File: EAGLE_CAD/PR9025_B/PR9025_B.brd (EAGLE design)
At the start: 70 x 70 mm, 75 parts, among them SW1 C&K_PTS645

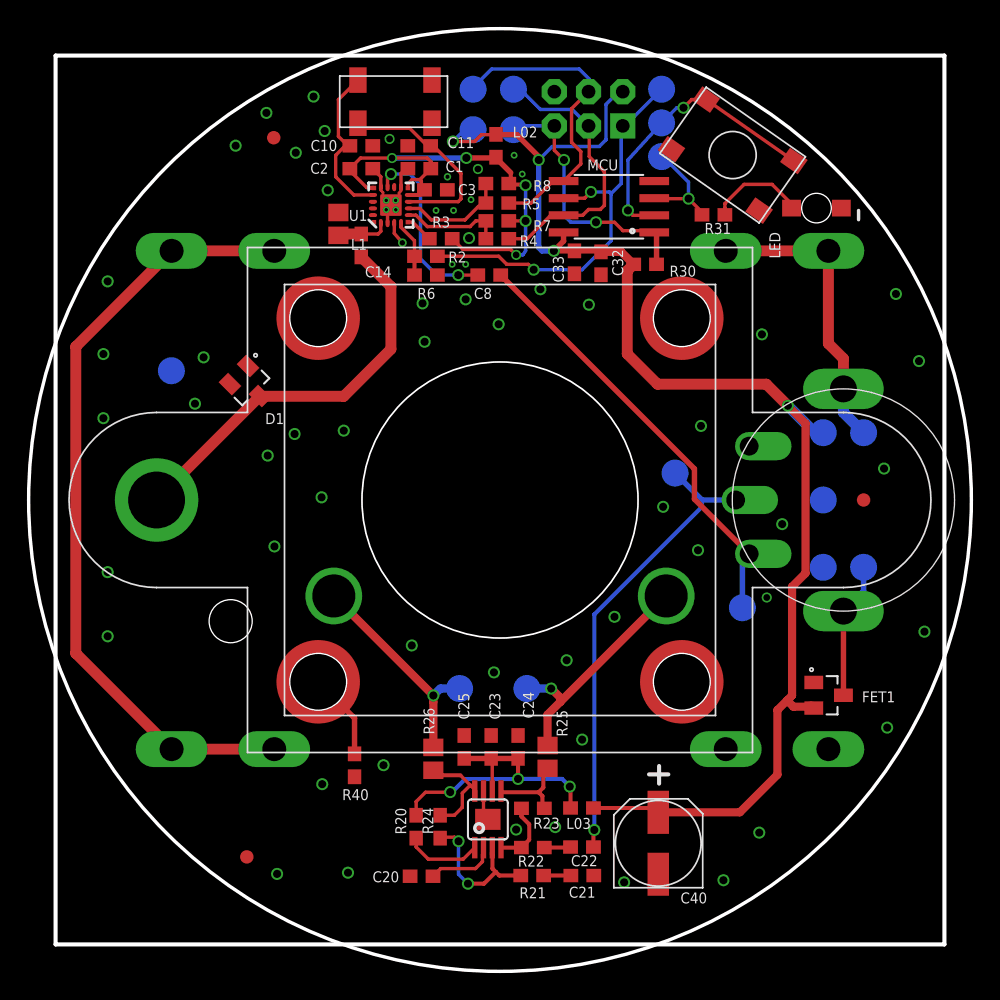
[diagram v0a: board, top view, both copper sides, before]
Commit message: PR9025_B
This is a WIP. 9025B will incorporate learnings from Josh’s 9025A
build, and most significantly update the ISP header to be centered on
the PCB at 35mm. There’s still routing and error checking to be done.
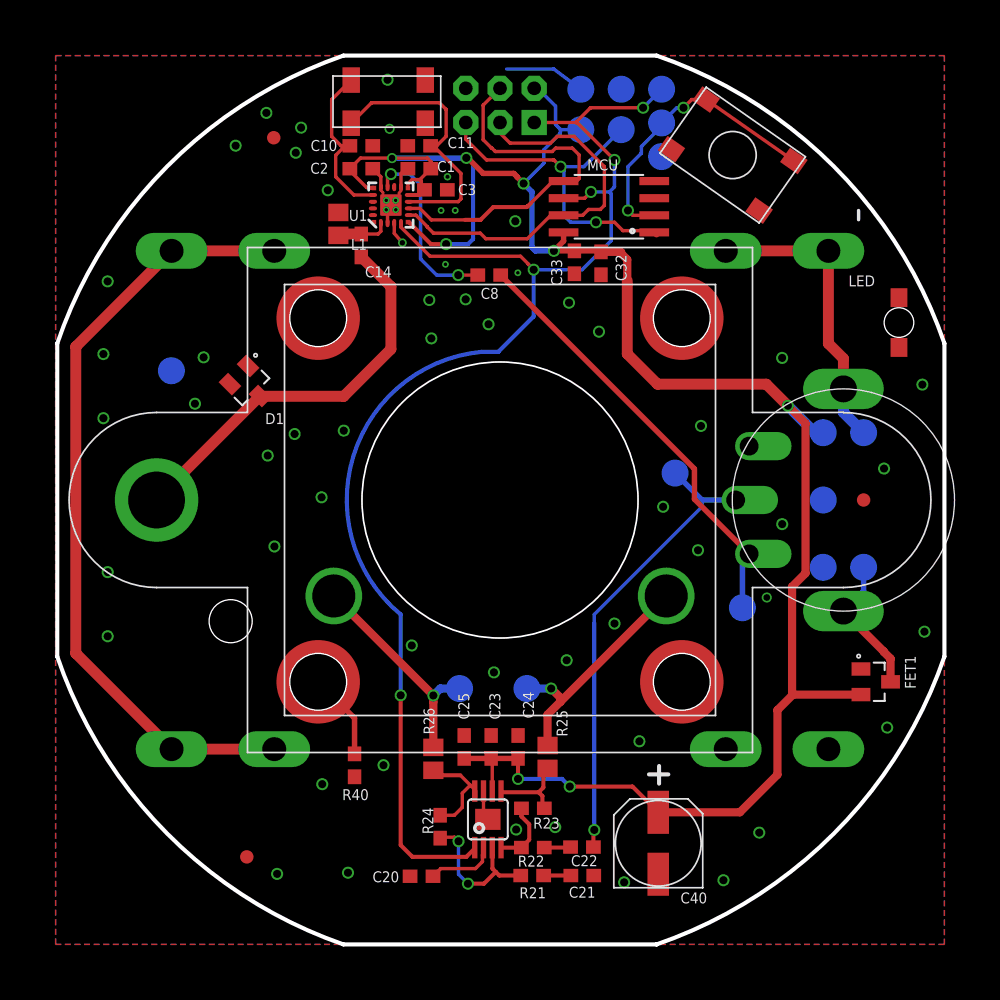
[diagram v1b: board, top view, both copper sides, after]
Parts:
- removed L02, L03: 2.2k@100MHz, PR_Parts_Library:0603_CPL
- removed R2, R4, R5: 330, PR_Parts_Library:0603_CPL
- removed R20, R30, R6: 10K, PR_Parts_Library:0603_CPL
- removed R3, R7, R8: 4.7K, PR_Parts_Library:0603_CPL
- removed R31: 1K, PR_Parts_Library:0603_CPL
- moved LED 10.5 mm to (64.6, 48.2), turned to 270 degrees
- moved T11 8.00 mm to (44.0, 65.5)
- moved T12 8.00 mm to (44.0, 62.5)
- moved T13 8.00 mm to (41.0, 65.5)
- moved T5 8.00 mm to (41.0, 62.5)
- moved ISP 6.58 mm to (35.0, 64.3)
- moved FET1 3.64 mm to (62.9, 21.5)
- moved X1 0.50 mm to (26.7, 64.6)
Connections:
- removed net !RST-L: R2.2, R6.2, U1.5
- removed net !SEN-L: R3.1, U1.6
- removed net 3.3V: C1.1, C2.1, C3.1, L02.2, R3.2, R7.2, R8.2, U1.10, U1.11, U1.16
- removed net N$2: AMP.6, C23.1, C24.1, C25.1, L03.2, R20.2
- removed net N$20: AMP.1, R20.1
- removed net N$7: LED.P$1, R31.1
- removed net SCLK-L: R4.2, R7.1, U1.7
- removed net SDIO-L: R5.2, R8.1, U1.8
- net !RST: now also AMP.1, U1.5; no longer R2.1
- net GND: no longer R6.1
- net LED/PB4: now also LED.P$1; no longer R31.2
- net RESET: no longer R30.2
- net SCLK: now also U1.7; no longer R4.1
- net SDIO: now also U1.8; no longer R5.1
- net VCC: now also AMP.6, C1.1, C2.1, C23.1, C24.1, C25.1, C3.1, U1.10, U1.11, U1.16, U1.6; no longer L02.1, L03.1, R30.1
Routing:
- net !RST: track 30.9 -> 95.1 mm, vias 2 -> 5
- net VCC: track 104.9 -> 150.8 mm, vias 4 -> 8
- net 3.3V: track 39.7 -> 0.00 mm, vias 5 -> 0
- net N$2: track 23.0 -> 0.00 mm, vias 3 -> 0
- net SDIO: track 23.3 -> 35.0 mm
- net N$7: track 8.20 -> 0.00 mm
- net LED/PB4: track 8.19 -> 0.00 mm, vias 1 -> 0
- net SDIO-L: track 8.10 -> 0.00 mm
- net SCLK: track 21.2 -> 29.1 mm
- net SCLK-L: track 7.57 -> 0.00 mm
- net RESET: track 19.8 -> 25.9 mm
- net N$20: track 5.73 -> 0.00 mm
- net N$1: track 15.2 -> 20.7 mm
- net !RST-L: track 4.28 -> 0.00 mm
- net !SEN-L: track 2.10 -> 0.00 mm
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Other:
- board size 70 x 70 mm -> 65.9 x 66 mm

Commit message: updated dimension layer, a few small trace changes
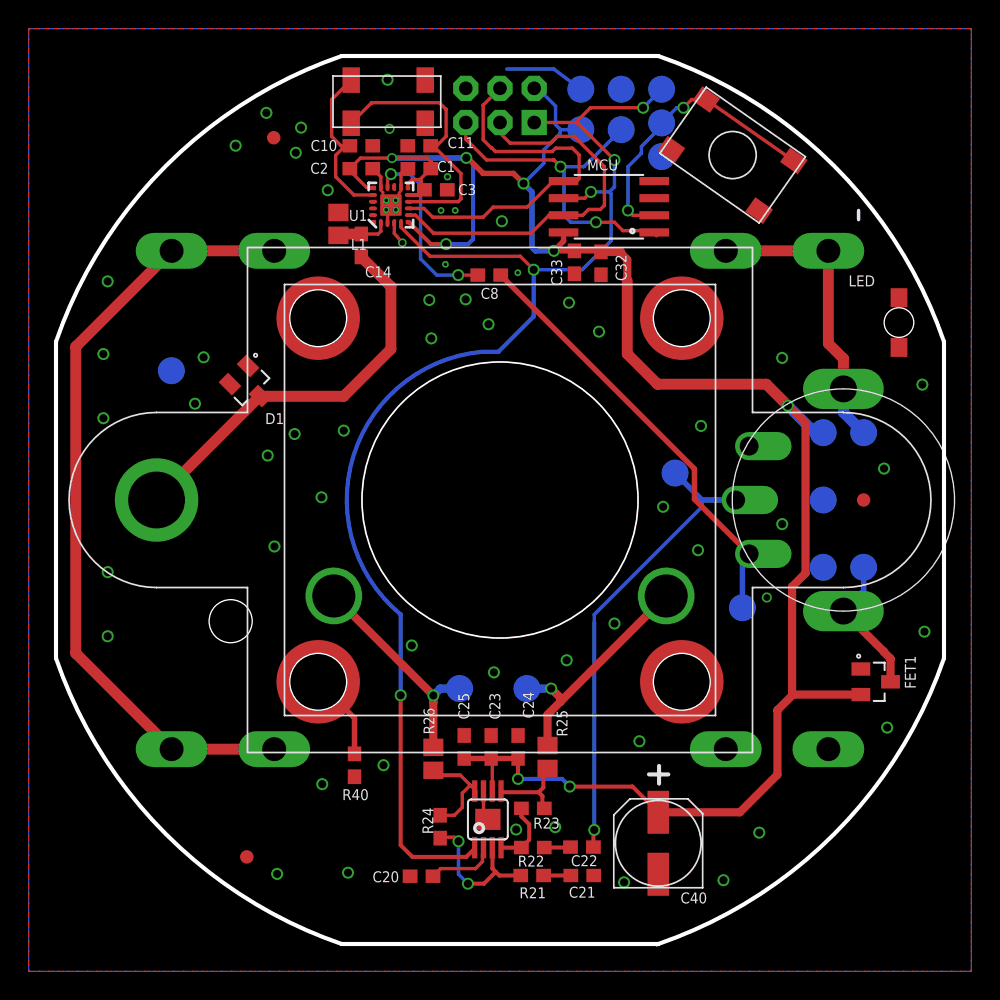
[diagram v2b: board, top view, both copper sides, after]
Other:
- outline, holes or cut-outs redrawn

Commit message: PR9025B
Centered ISP header and finished layout.
Moved optimized placement for reverse mount LED
Removed R40 and made a short
Optimized vias placements
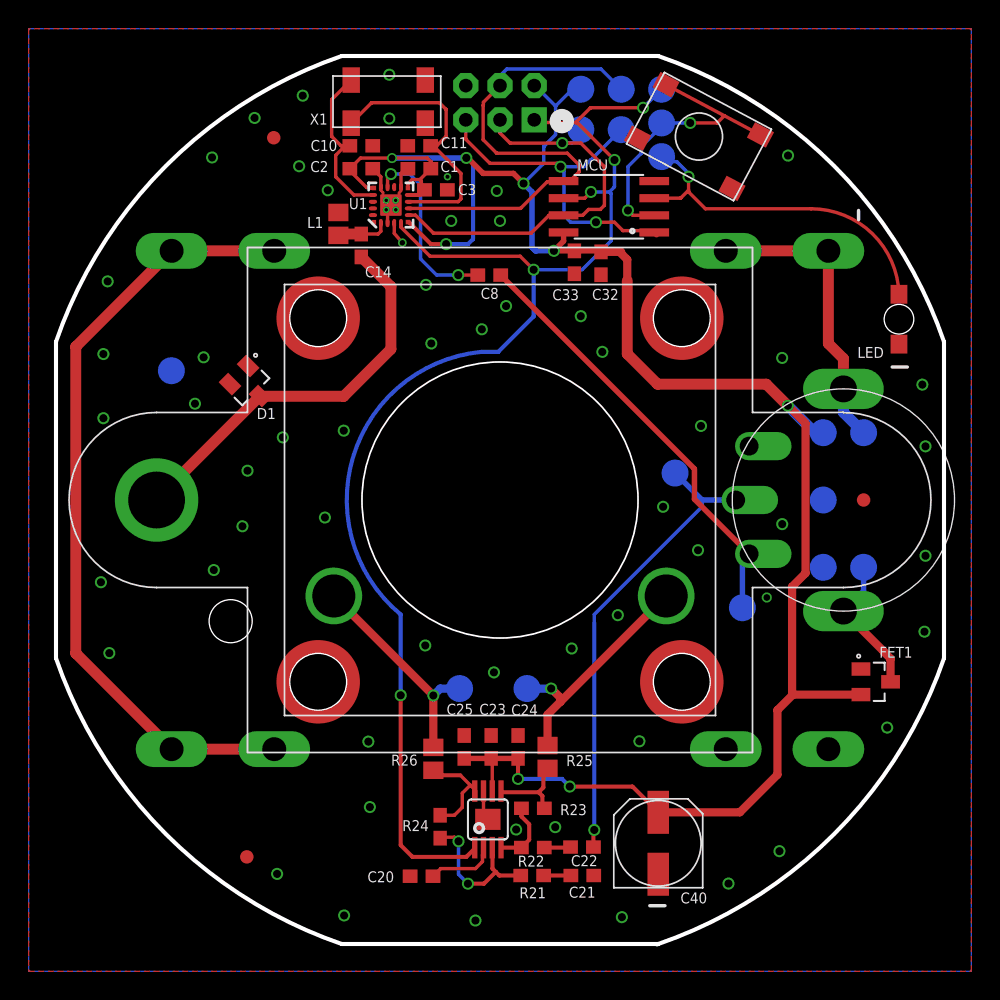
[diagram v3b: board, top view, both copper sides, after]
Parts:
- removed R40: DNP, PR_Parts_Library:0603_CPL
- moved T11 4.24 mm to (41.0, 62.5)
- moved T13 3.00 mm to (44.0, 65.5)
- moved T5 3.00 mm to (41.0, 65.5)
- moved SW1 2.85 mm to (49.8, 62.0), turned to 152 degrees
- moved LED 0.25 mm to (64.6, 48.4)
- moved ISP 0.20 mm to (35.0, 64.5)
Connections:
- removed net N$6: R40.1, U$5.P$1
- net GND: now also U$5.P$1; no longer R40.2
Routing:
- net LED/PB4: track 0.00 -> 25.4 mm, vias 0 -> 1
- net N$6: track 6.47 -> 0.00 mm
- net SDIO: track 35.0 -> 37.2 mm
- net SCLK: track 28.8 -> 30.6 mm, vias 0 -> 1
- net SW: track 22.5 -> 23.4 mm
- net VCC: track 150.8 -> 151.4 mm
- net GND: vias 60 -> 62
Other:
- board text added: "PR9025B Born + tuned in Brooklyn http://thepublicrad.io"
- board text added: "X1"
- board text removed: "PR9024 Born + tuned in Brooklyn http://thepublicrad.io"
